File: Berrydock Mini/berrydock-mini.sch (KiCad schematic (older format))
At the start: 86 parts, among them J1 RJ45, P1 CONN_01X16, P2 CONN_01X07, P3 CONN_01X04, P4 CONN_01X03, P5 USB_OTG, P6 USB_A, SW1 SWITCH_INV, SW2 BUTTON, U1 CP2102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

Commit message: final touches
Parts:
- added G1: SIMPLELOGO, Omega2-Berrydock:simplelogo, symbol SIMPLELOGO
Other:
- note added: "Select 5V Source:\nUSB or ETH or LIPO\n"
- note removed: "Select 5V Source:\nETH or USB or LIPO\n"
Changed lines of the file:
@@
 $EndComp
 Text Notes 9650 2300 0    60   ~ 0
-Select 5V Source:\nETH or USB or LIPO\n
+Select 5V Source:\nUSB or ETH or LIPO\n
 Text Notes 6500 1050 0    60   ~ 0
 ETH to 5V Regulator
@@
 NoConn ~ 14350 6650
 NoConn ~ 14350 6550
+$Comp
+L SIMPLELOGO G1
+U 1 1 57EEE161
+P 12750 9500
+F 0 "G1" H 12750 9280 60  0001 C CNN
+F 1 "SIMPLELOGO" H 12750 9720 60  0001 C CNN
+F 2 "Omega2-Berrydock:simplelogo" H 12750 9500 60  0001 C CNN
+F 3 "" H 12750 9500 60  0001 C CNN
+	1    12750 9500
+	1    0    0    -1
+$EndComp
 $EndSCHEMATC

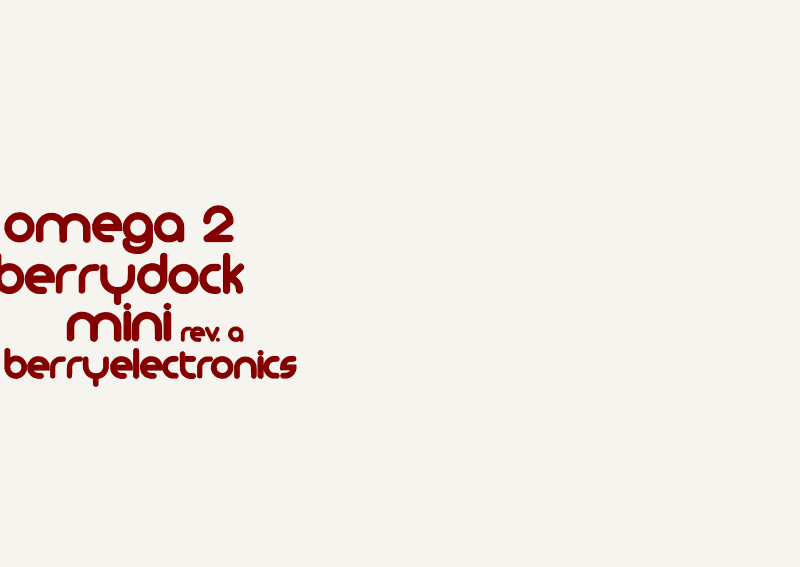
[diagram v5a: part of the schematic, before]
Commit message: added OSHWLOGO
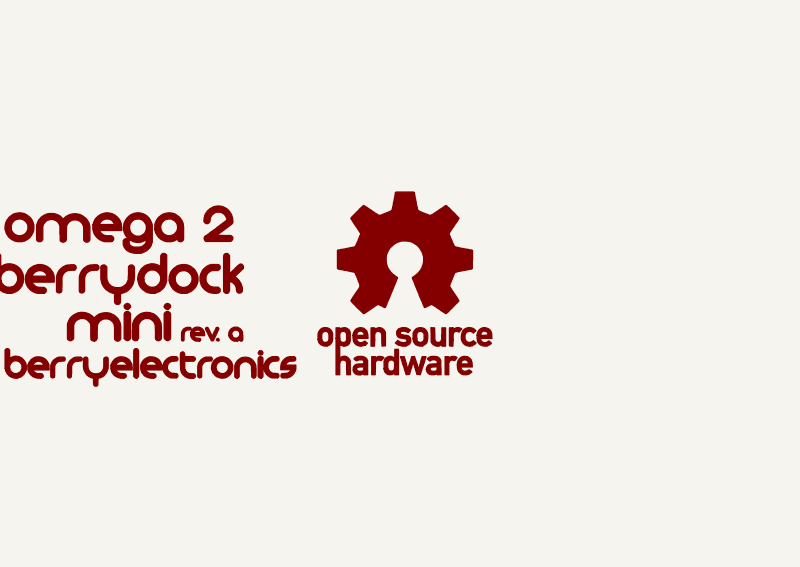
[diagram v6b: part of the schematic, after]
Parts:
- added G2: OSHWLOGO, Omega2-Berrydock:oshwlogo, symbol OSHWLOGO
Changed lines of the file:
@@
+	1    0    0    -1
+$EndComp
+$Comp
+L OSHWLOGO G2
+U 1 1 57EEDA5B
+P 14000 9450
+F 0 "G2" H 14000 9080 60  0001 C CNN
+F 1 "OSHWLOGO" H 14000 9820 60  0001 C CNN
+F 2 "Omega2-Berrydock:oshwlogo" H 14000 9450 60  0001 C CNN
+F 3 "" H 14000 9450 60  0001 C CNN
+	1    14000 9450
 	1    0    0    -1
 $EndComp
